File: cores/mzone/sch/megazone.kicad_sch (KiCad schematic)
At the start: 8 parts

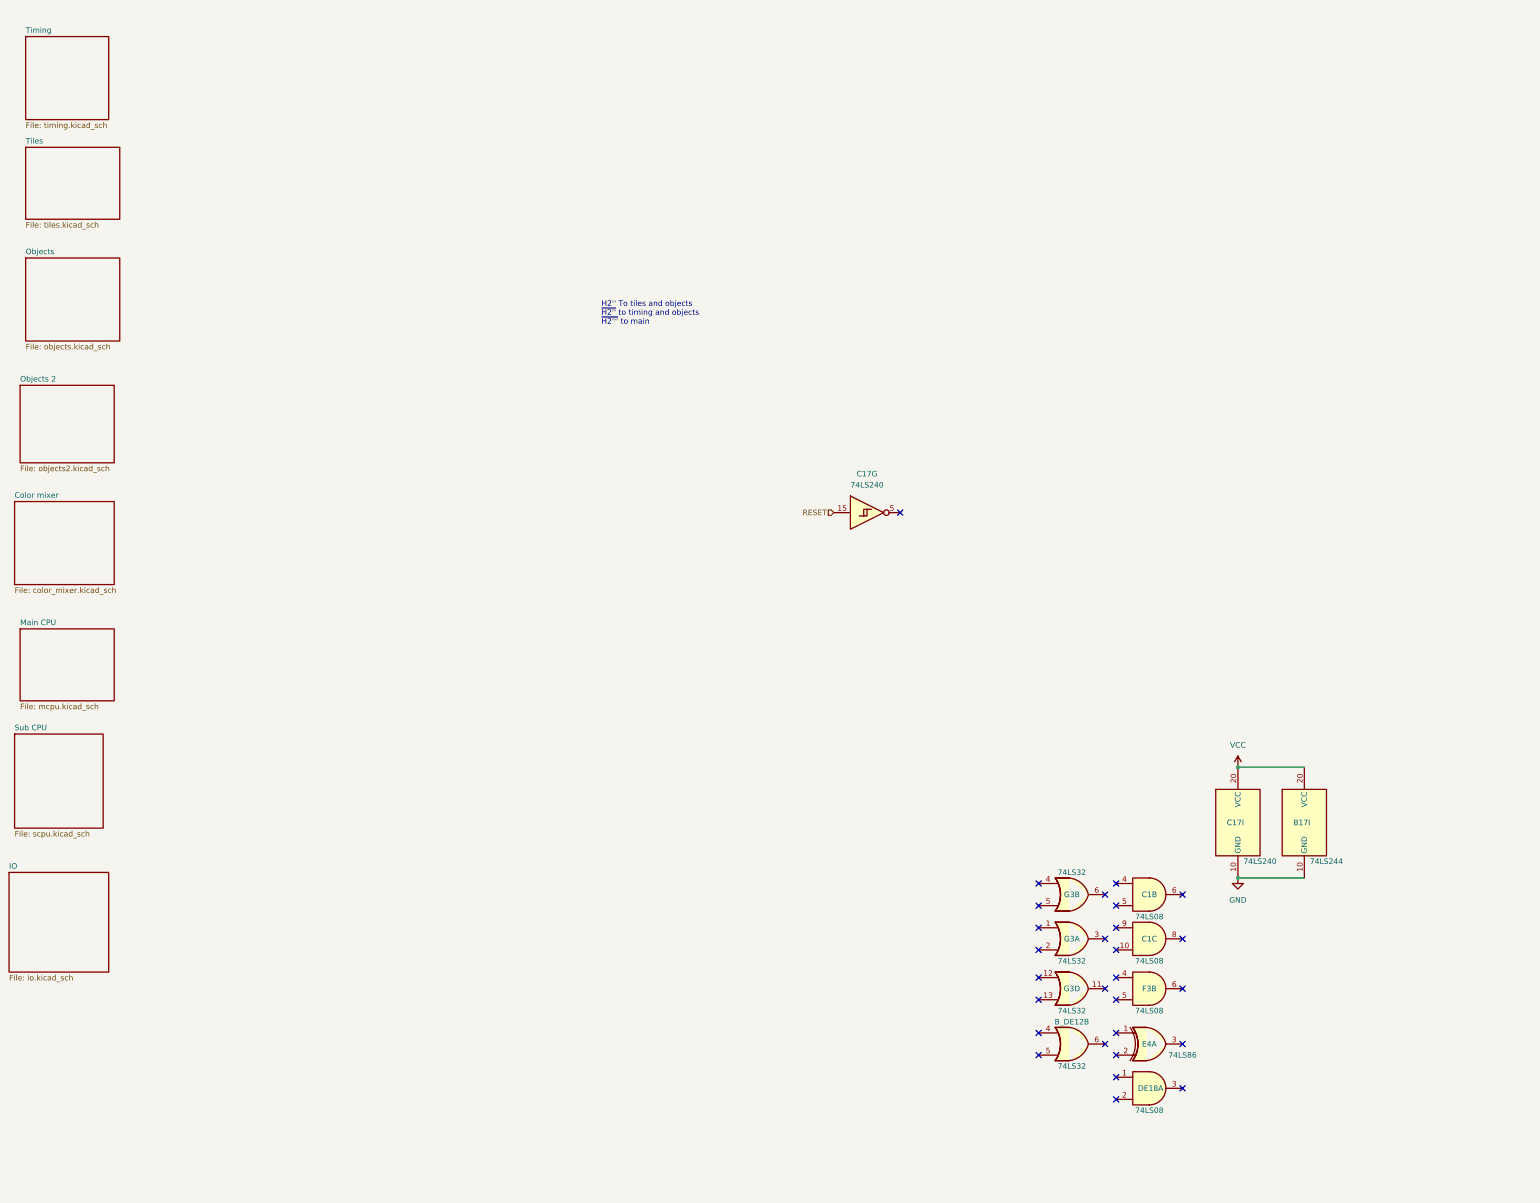
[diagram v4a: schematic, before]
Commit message: mzone core
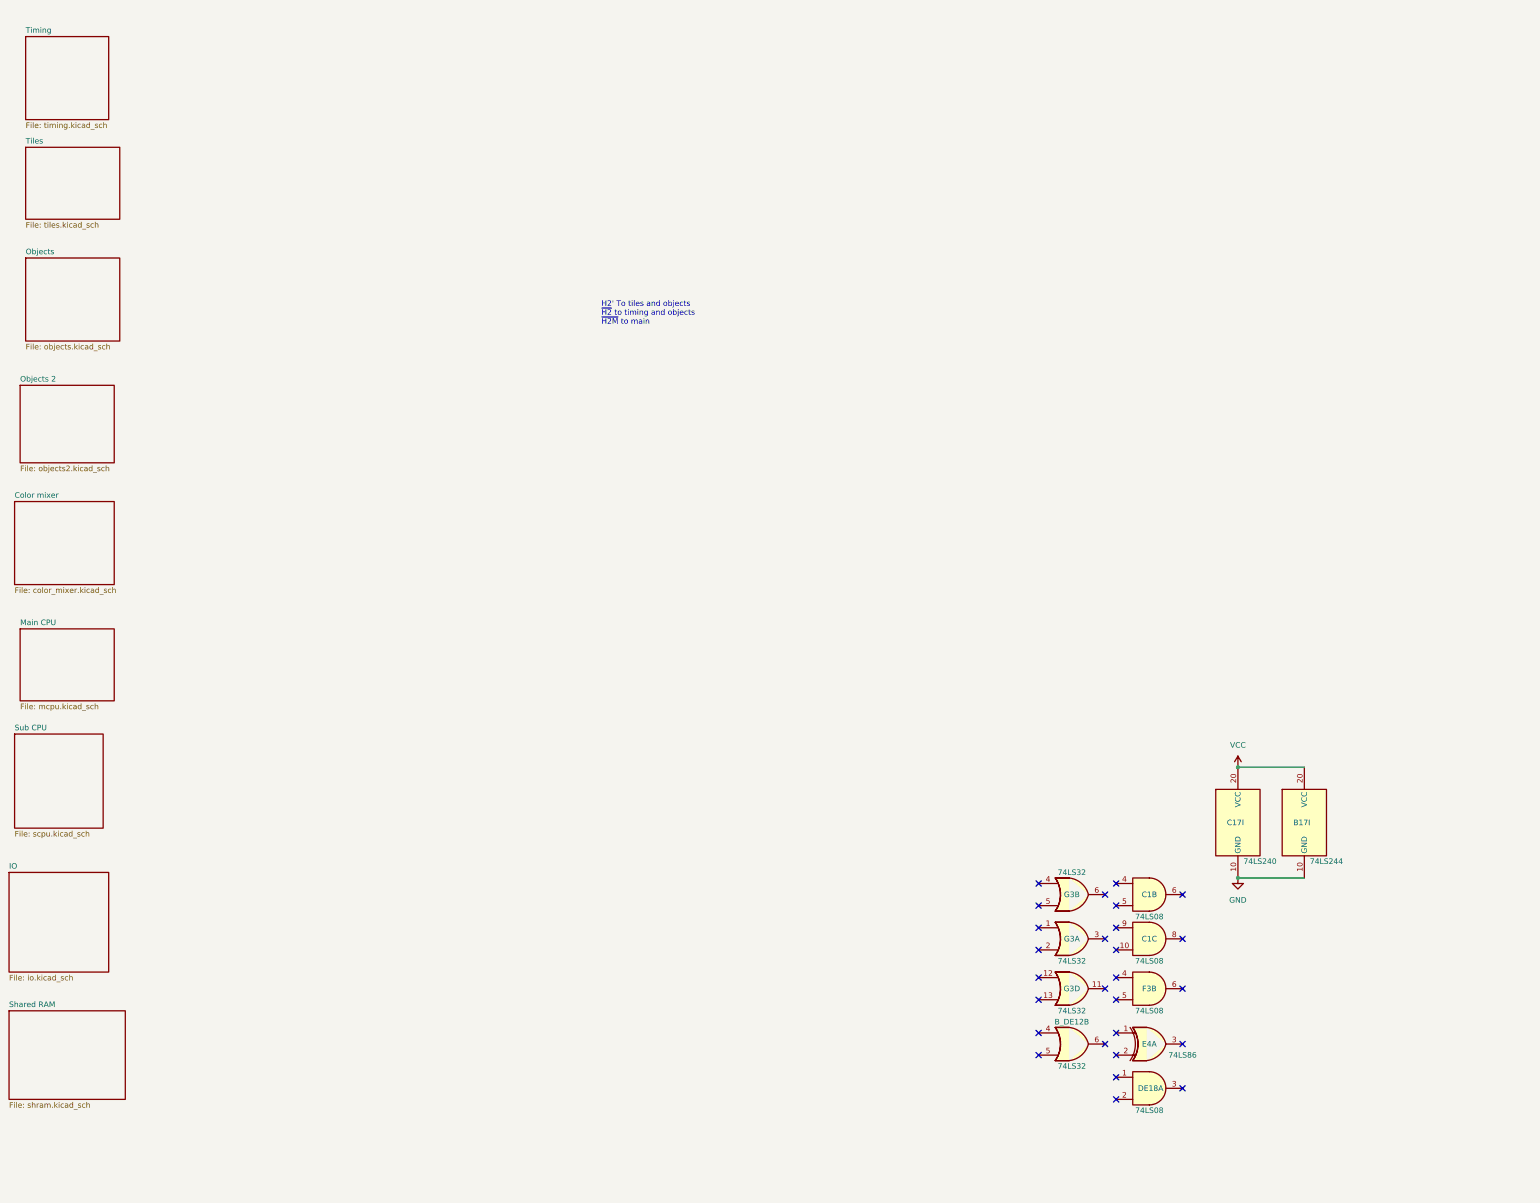
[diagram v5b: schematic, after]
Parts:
- removed unit 7 of C17
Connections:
- no-connect marks 28 -> 27
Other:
- added sheet Shared RAM (shram.kicad_sch)
- note added: "H2' To tiles and objects ~{H2} to timing and objects ~{H2M} to main"
- note removed: "H2'' To tiles and objects ~{H2''} to timing and objects ~{H2'''} to main"
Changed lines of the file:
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@@
-	)
-	(no_connect
-		(at 227.33 134.62)
 	)
 	(no_connect
@@
 		)
 	)
-	(text "H2'' To tiles and objects\n~{H2''} to timing and objects\n~{H2'''} to main"
+	(text "H2' To tiles and objects\n~{H2} to timing and objects\n~{H2M} to main"
 		(exclude_from_sim no)
 		(at 158.75 88.9 0)
@@
 			)
 			(justify left)
-		)
-	)
-	(hierarchical_label "RESET"
-		(shape input)
-		(at 212.09 134.62 180)
-		(effects
-			(font
-				(size 1.27 1.27)
-			)
-			(justify right)
 		)
 	)
@@
 	(symbol
 		(lib_id "74xx:74LS240_Split")
-		(at 219.71 134.62 0)
-		(unit 7)
-		(exclude_from_sim no)
-		(in_bom yes)
-		(on_board yes)
-		(dnp no)
-		(fields_autoplaced yes)
-		(property "Reference" "C17"
-			(at 219.71 125.73 0)
-			(effects
-				(font
-					(size 1.27 1.27)
-				)
-			)
-		)
-		(property "Value" "74LS240"
-			(at 219.71 128.27 0)
-			(effects
-				(font
-					(size 1.27 1.27)
-				)
-			)
-		)
-		(property "Footprint" ""
-			(at 219.71 134.62 0)
-			(effects
-				(font
-					(size 1.27 1.27)
-				)
-				(hide yes)
-			)
-		)
-		(property "Datasheet" "http://www.ti.com/lit/ds/symlink/sn74ls240.pdf"
-			(at 219.71 134.62 0)
-			(effects
-				(font
-					(size 1.27 1.27)
-				)
-				(hide yes)
-			)
-		)
-		(property "Description" "Octal Buffer and Line Driver With 3-State Output, active-low enables, inverting outputs, split symbol"
-			(at 219.71 134.62 0)
-			(effects
-				(font
-					(size 1.27 1.27)
-				)
-				(hide yes)
-			)
-		)
-		(pin "20"
-		)
-		(pin "19"
-		)
-		(pin "11"
-		)
-		(pin "7"
-		)
-		(pin "10"
-		)
-		(pin "13"
-		)
-		(pin "12"
-		)
-		(pin "14"
-		)
-		(pin "15"
-		)
-		(pin "16"
-		)
-		(pin "17"
-		)
-		(pin "3"
-		)
-		(pin "1"
-		)
-		(pin "2"
-		)
-		(pin "18"
-		)
-		(pin "5"
-		)
-		(pin "4"
-		)
-		(pin "6"
-		)
-		(pin "8"
-		)
-		(pin "9"
-		)
-		(instances
-			(project ""
-				(path "/b3e039a8-74b0-4cb4-b612-5df1f0b42747"
-					(reference "C17")
-					(unit 7)
-				)
-			)
-		)
-	)
-	(symbol
-		(lib_id "74xx:74LS240_Split")
 		(at 304.8 205.74 0)
 		(unit 9)
@@
 				)
 			)
+		)
+	)
+	(sheet
+		(at 22.86 248.92)
+		(size 26.67 20.32)
+		(fields_autoplaced yes)
+		(stroke
+			(width 0.1524)
+			(type solid)
+		)
+		(fill
+			(color 0 0 0 0.0000)
+		)
+		(property "Sheetname" "Shared RAM"
+			(at 22.86 248.2084 0)
+			(effects
+				(font
+					(size 1.27 1.27)
+				)
+				(justify left bottom)
+			)
+		)
+		(property "Sheetfile" "shram.kicad_sch"
+			(at 22.86 269.8246 0)
+			(effects
+				(font
+					(size 1.27 1.27)
+				)
+				(justify left top)
+			)
+		)
+		(instances
+			(project "megazone"
+				(path "/b3e039a8-74b0-4cb4-b612-5df1f0b42747"
+					(page "10")
+				)
+			)

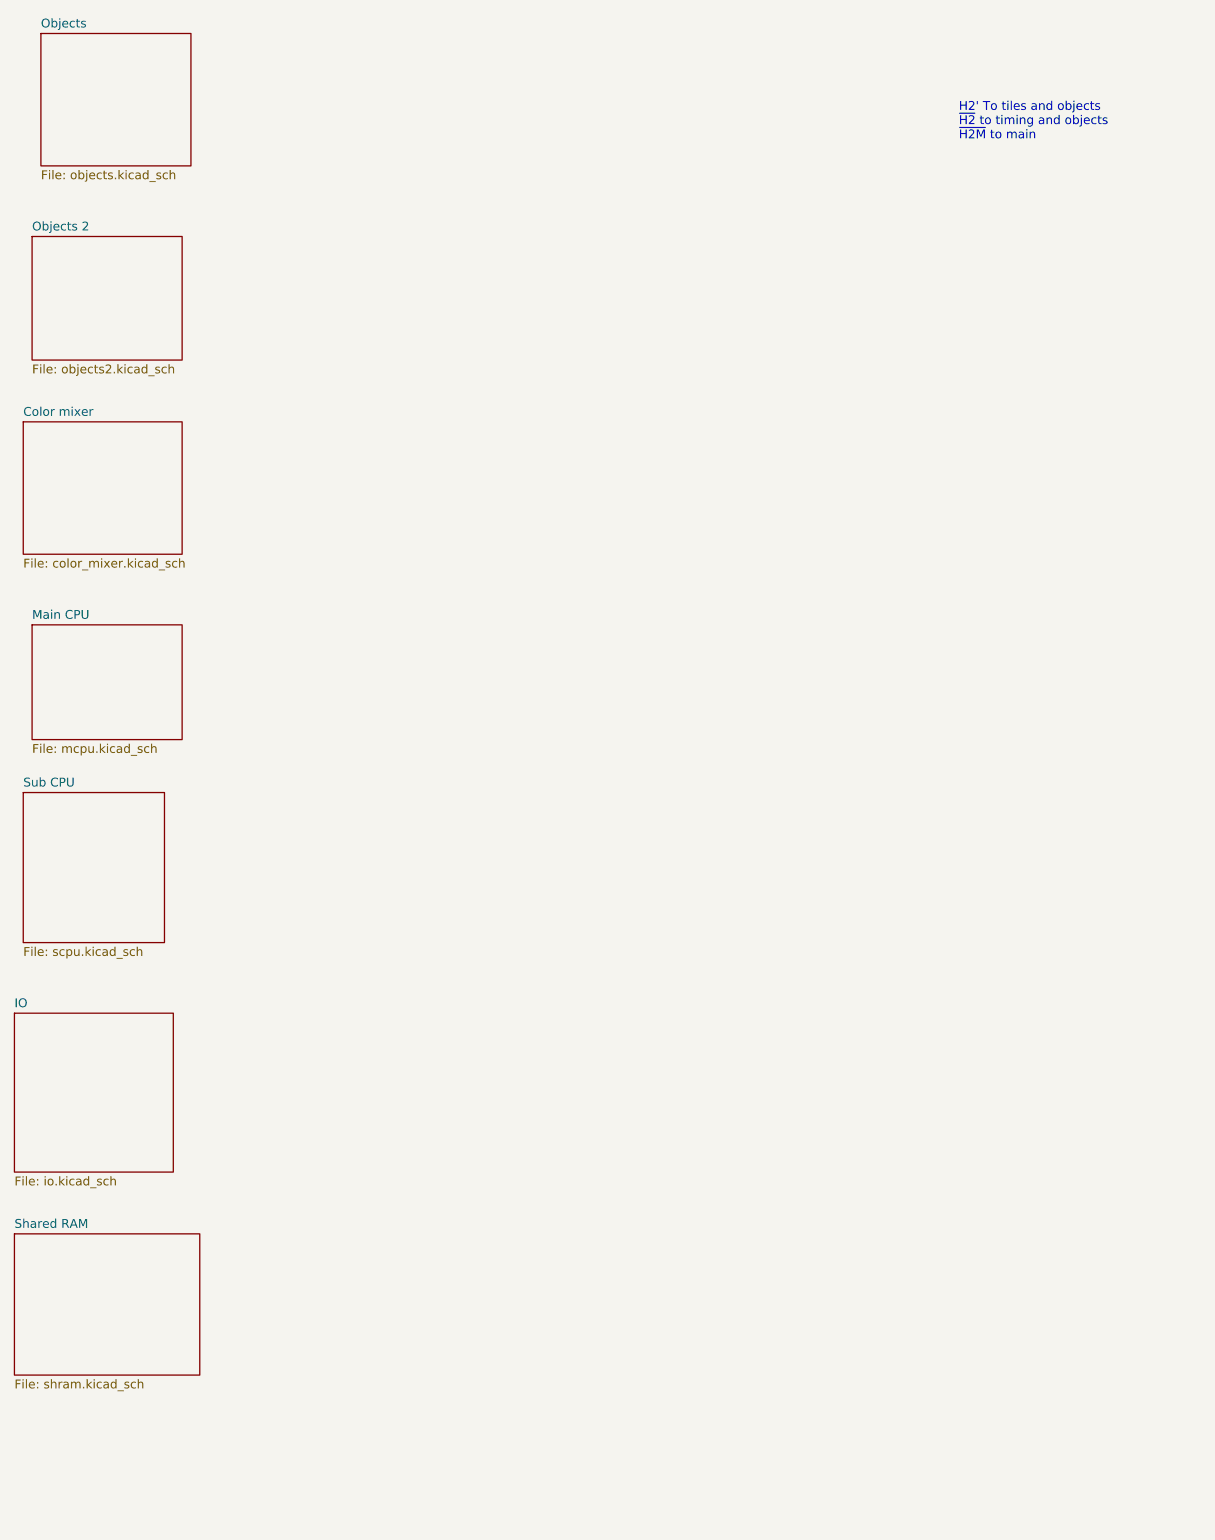
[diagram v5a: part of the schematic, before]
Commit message: mzone core
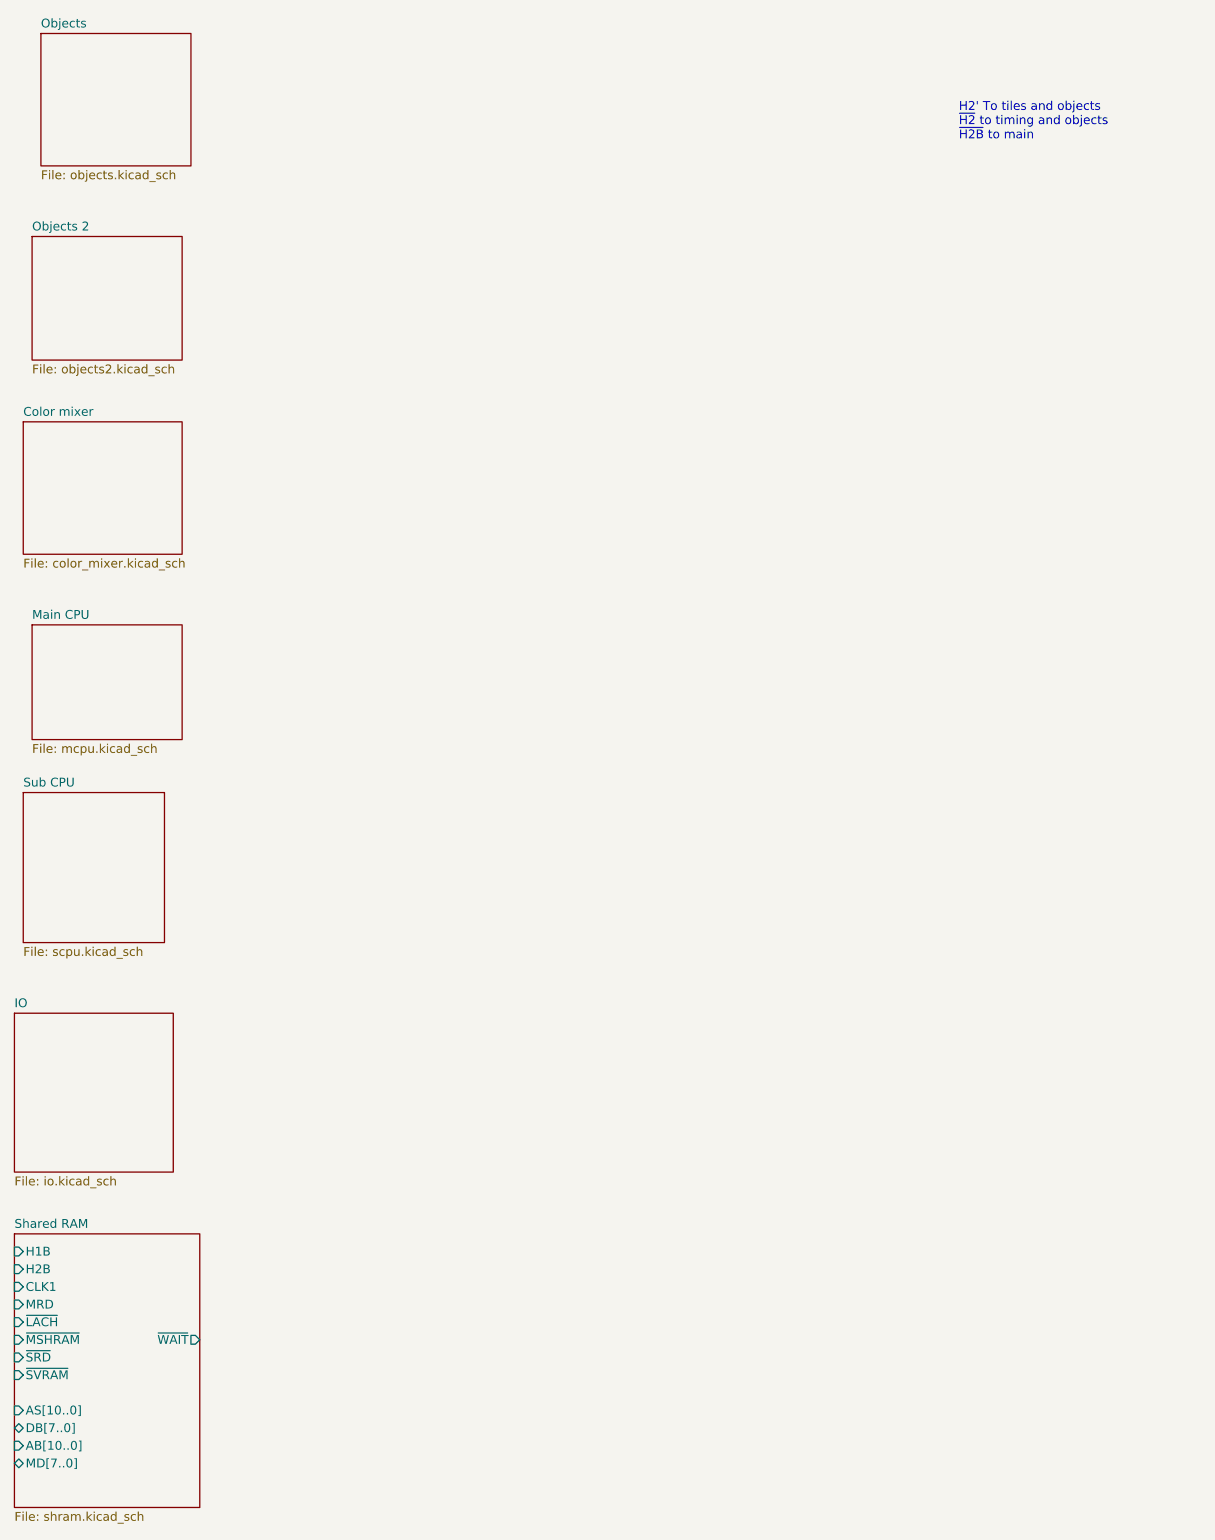
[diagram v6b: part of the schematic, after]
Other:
- sheet Shared RAM ports: added AB[10..0], AS[10..0], CLK1, DB[7..0], H1B, H2B, MD[7..0], MRD, ~{LACH}, ~{MSHRAM}, ~{SRD}, ~{SVRAM}, ~{WAIT}; removed none
- note added: "H2' To tiles and objects ~{H2} to timing and objects ~{H2B} to main"
- note removed: "H2' To tiles and objects ~{H2} to timing and objects ~{H2M} to main"
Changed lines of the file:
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@@
 		)
 	)
-	(text "H2' To tiles and objects\n~{H2} to timing and objects\n~{H2M} to main"
+	(text "H2' To tiles and objects\n~{H2} to timing and objects\n~{H2B} to main"
 		(exclude_from_sim no)
 		(at 158.75 88.9 0)
@@
 	(sheet
 		(at 22.86 248.92)
-		(size 26.67 20.32)
+		(size 26.67 39.37)
 		(fields_autoplaced yes)
 		(stroke
@@
 		)
 		(property "Sheetfile" "shram.kicad_sch"
-			(at 22.86 269.8246 0)
+			(at 22.86 288.8746 0)
 			(effects
 				(font
@@
 			)
 		)
+		(pin "H2B" input
+			(at 22.86 254 180)
+			(effects
+				(font
+					(size 1.27 1.27)
+				)
+				(justify left)
+			)
+		)
+		(pin "MRD" input
+			(at 22.86 259.08 180)
+			(effects
+				(font
+					(size 1.27 1.27)
+				)
+				(justify left)
+			)
+		)
+		(pin "~{LACH}" input
+			(at 22.86 261.62 180)
+			(effects
+				(font
+					(size 1.27 1.27)
+				)
+				(justify left)
+			)
+		)
+		(pin "~{MSHRAM}" input
+			(at 22.86 264.16 180)
+			(effects
+				(font
+					(size 1.27 1.27)
+				)
+				(justify left)
+			)
+		)
+		(pin "H1B" input
+			(at 22.86 251.46 180)
+			(effects
+				(font
+					(size 1.27 1.27)
+				)
+				(justify left)
+			)
+		)
+		(pin "~{WAIT}" output
+			(at 49.53 264.16 0)
+			(effects
+				(font
+					(size 1.27 1.27)
+				)
+				(justify right)
+			)
+		)
+		(pin "DB[7..0]" bidirectional
+			(at 22.86 276.86 180)
+			(effects
+				(font
+					(size 1.27 1.27)
+				)
+				(justify left)
+			)
+		)
+		(pin "~{SRD}" input
+			(at 22.86 266.7 180)
+			(effects
+				(font
+					(size 1.27 1.27)
+				)
+				(justify left)
+			)
+		)
+		(pin "~{SVRAM}" input
+			(at 22.86 269.24 180)
+			(effects
+				(font
+					(size 1.27 1.27)
+				)
+				(justify left)
+			)
+		)
+		(pin "CLK1" input
+			(at 22.86 256.54 180)
+			(effects
+				(font
+					(size 1.27 1.27)
+				)
+				(justify left)
+			)
+		)
+		(pin "AB[10..0]" input
+			(at 22.86 279.4 180)
+			(effects
+				(font
+					(size 1.27 1.27)
+				)
+				(justify left)
+			)
+		)
+		(pin "MD[7..0]" bidirectional
+			(at 22.86 281.94 180)
+			(effects
+				(font
+					(size 1.27 1.27)
+				)
+				(justify left)
+			)
+		)
+		(pin "AS[10..0]" input
+			(at 22.86 274.32 180)
+			(effects
+				(font
+					(size 1.27 1.27)
+				)
+				(justify left)
+			)
+		)
